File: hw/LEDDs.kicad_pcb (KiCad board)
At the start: 2 copper layers, 95 x 46 mm, 87 parts, among them J1 Screw_Terminal_01x02, J2 Conn_01x01, J3 Conn_01x06, J4 Screw_Terminal_01x02, K1 Relay_DPDT, Q10 MMBT3904, Q11 MMBT3906, Q13 IPN80R900P7, Q14 IPN80R900P7, Q2 BC846SF, Q8 MMBT3904, Q9 MMBT3904, U1 esp-12f, U2 PC817XI, U3 H11L1SR2M, U4 PC817XI

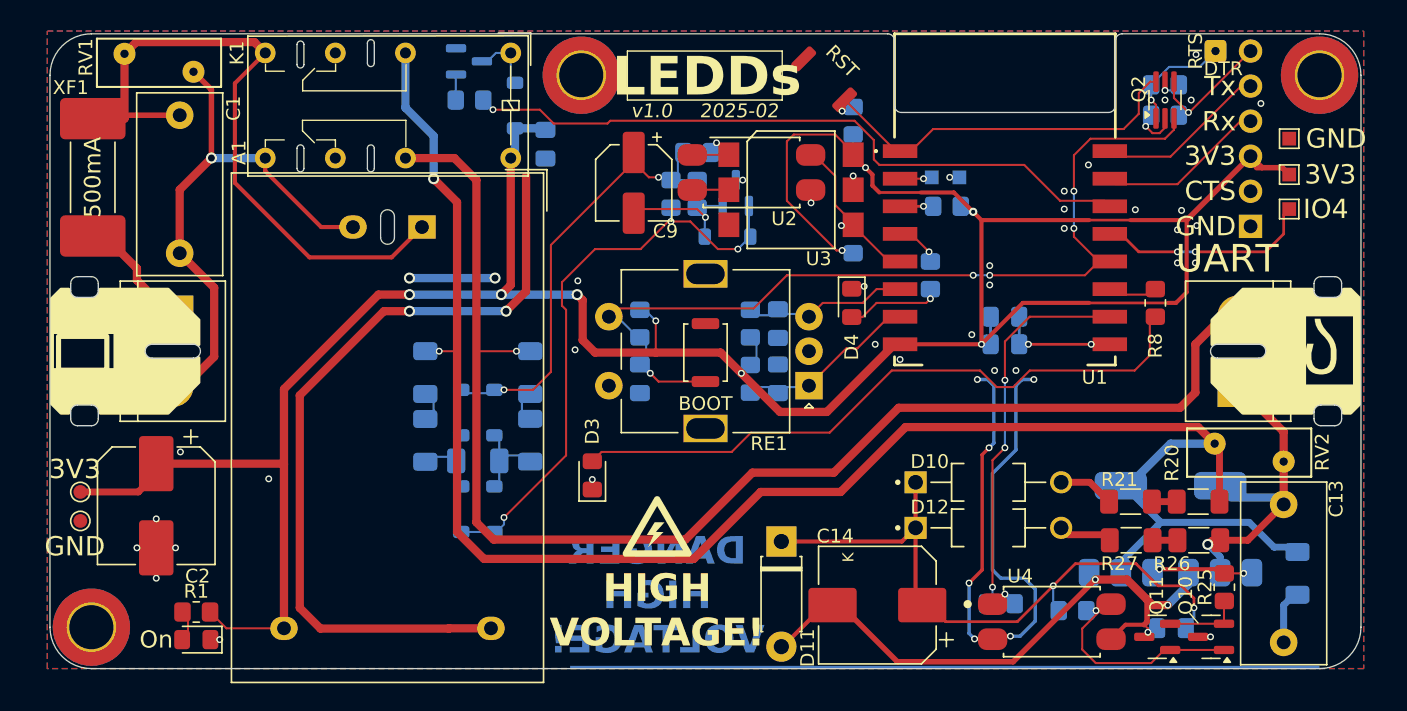
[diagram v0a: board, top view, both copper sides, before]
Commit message: V2.0 (#2)
* **Hardware & Mechanical Design**
  * Updated design files and exports.
  * Split chassis and top plate into variants.
  * Changed enclosure folder structure.
  * Hid alignment/dimension layers; removed duplicate models.
  * Added mechanical parts and notes to schematics.

* **Firmware**
  * Updated firmware and added new versions.
  * Introduced firmware variants and consolidated them into packages.
  * Added common.yaml.
  * Moved effects out of packages.

* **Project Structure & Tooling**
  * Added BOM exports and fixed script permissions.
  * Updated and cleaned export folders.
  * Added ESPHome auto-generated `.gitignore`.
  * Fixed included libraries.
  * Miscellaneous corrections, reviews, merges, and cleanup commits.

* **Documentation & README**
  * Multiple revisions for clarity, formatting, structure, and consistency.
  * Added safety warnings for mains voltage operation.
  * Updated table of contents, badges, links, images, and repository structure sections.
  * Added roadmap, split release and change logs, reformatted release log.
  * Added links to schematic, PCB, BOMs, and iBOM.
  * Added additional documentation files.

* **Images, Photos & Media**
  * Updated, renamed, resized, and reformatted images.
  * Improved README image layout (width adjustments, centering, reduced size).
  * Added photos and screenshots across README and sub-readmes.
  * Added animations and animation exports; removed obsolete images.
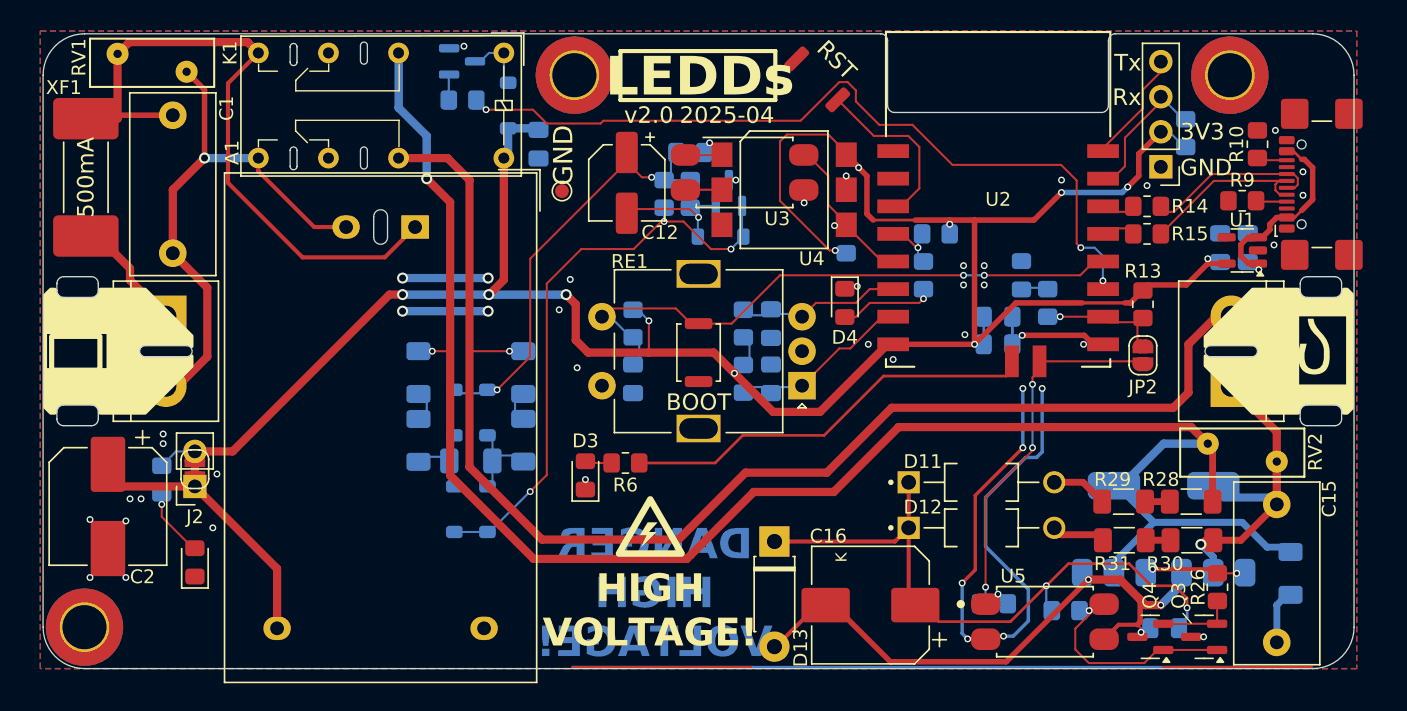
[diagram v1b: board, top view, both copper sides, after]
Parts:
- removed the Q2 at (133.3, 56.8)
- removed the R6 at (133.3, 57.9)
- removed the R7 at (133.3, 55.7)
- removed the TP1 at (54.7, 85.2)
- removed TP3: 3V3, TestPoint:TestPoint_Pad_1.0x1.0mm
- removed TP4: ADC, TestPoint:TestPoint_Pad_1.0x1.0mm
- removed TP5: GPIO4, TestPoint:TestPoint_Pad_1.0x1.0mm
- removed TP6, TP7: GND, TestPoint:TestPoint_Pad_1.0x1.0mm
- added C7: 1u, Capacitor_SMD:C_0805_2012Metric_Pad1.18x1.45mm_HandSolder, B.Cu at (139.3, 67.5)
- added C8: 1u, Capacitor_SMD:C_0805_2012Metric_Pad1.18x1.45mm_HandSolder, B.Cu at (137.3, 67.5)
- added D5: ~, LED_SMD:LED_0805_2012Metric_Pad1.15x1.40mm_HandSolder, B.Cu at (122.9, 69.5)
- added J3: USB_C_Receptacle_USB2.0_14P, Connector_USB:USB_C_Receptacle_GCT_USB4110, F.Cu at (145.8, 62.9)
- added JP1: SolderJumper_2_Bridged, Jumper:SolderJumper-2_P1.3mm_Bridged_RoundedPad1.0x1.5mm, F.Cu at (63.0, 83.5)
- added JP2: SolderJumper_2_Open, Jumper:SolderJumper-2_P1.3mm_Open_RoundedPad1.0x1.5mm, F.Cu at (131.7, 75.3)
- added R12: 20k, Resistor_SMD:R_0805_2012Metric_Pad1.20x1.40mm_HandSolder, B.Cu at (134.8, 59.2)
- added R13: 20k, Resistor_SMD:R_0805_2012Metric_Pad1.20x1.40mm_HandSolder, F.Cu at (131.7, 71.6)
- added R14: 0, Resistor_SMD:R_0805_2012Metric_Pad1.20x1.40mm_HandSolder, F.Cu at (132.0, 64.5)
- added R15: 0, Resistor_SMD:R_0805_2012Metric_Pad1.20x1.40mm_HandSolder, F.Cu at (132.0, 66.5)
- added R8: 240, Resistor_SMD:R_0805_2012Metric_Pad1.20x1.40mm_HandSolder, B.Cu at (124.8, 71.5)
- added R9: 5k1, Resistor_SMD:R_0805_2012Metric_Pad1.20x1.40mm_HandSolder, F.Cu at (138.9, 64.1)
- added U2: ESP32-C3-12F, ESP32-C3-12F:ESP32-C3-12F_RFS, F.Cu at (121.2, 64.0)
- C9: renamed from C8; value 100n -> 1u
- H1, H2, H3: value mounting hole -> 20mm
- J2: value Conn_01x01 -> Conn_01x02_Pin; footprint Connector_Wire:SolderWire-0.1sqmm_1x01_D0.4mm_OD1mm -> Connector_PinSocket_2.54mm:PinSocket_1x02_P2.54mm_Vertical
- J4: renamed from J3; footprint Connector_PinHeader_2.54mm:PinHeader_1x06_P2.54mm_Vertical -> Connector_PinHeader_2.54mm:PinHeader_1x04_P2.54mm_Vertical
- R1: value 120 -> 330; moved to B.Cu
- R10: value 20k -> 5k1; moved to F.Cu
- R16: renamed from R14; value 90k -> 91k
- R17: renamed from R15; value 90k -> 91k
- R18, R19: value 90k -> 91k
- RV1, RV2: value ~ -> 275V
- U1: value esp-12f -> AP2112K-3.3; footprint ESP-12F:esp12f -> Package_TO_SOT_SMD:SOT-23-5
- moved J2 80.4 mm to (63.0, 84.8), turned to 180 degrees
- moved TP1 42.3 mm to (89.6, 63.4), turned to 90 degrees
- moved R6 40.1 mm to (94.2, 83.1), turned to 0 degrees
- moved R10 29.3 mm to (140.0, 60.0), turned to 90 degrees
- moved U1 17.6 mm to (138.9, 67.7), turned to 180 degrees
- moved R1 9.92 mm to (60.6, 84.3), turned to 90 degrees
- moved J4 7.80 mm to (133.0, 61.6)
- moved H2 6.50 mm to (138.0, 55.0)
- moved D1 5.60 mm to (63.0, 90.3), turned to 90 degrees
- moved C2 3.50 mm to (56.7, 86.2)
- moved R11 2.15 mm to (116.7, 66.5)
- moved A1 0.50 mm to (79.0, 66.0)
- moved C1 0.50 mm to (61.4, 57.9)
- moved C10 0.50 mm to (121.2, 74.5)
- moved C11 0.50 mm to (83.0, 83.0)
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- renumbered C7 to C10, C10 to C11, C9 to C12, C11 to C13, C12 to C14, C13 to C15, C14 to C16, C5 to C4, C6 to C5, C4 to C6, D7 to D10, D10 to D11, D11 to D13, D5 to D6, D6 to D7, J4 to J5, Q8 to Q1, Q9 to Q2, Q10 to Q3, Q11 to Q4, Q13 to Q5, Q14 to Q6, R17 to R20, R16 to R21, R13 to R22, R12 to R23, R22 to R25, R25 to R26, R23 to R27, R20 to R28, R21 to R29, R26 to R30, R27 to R31, R8 to R6, R9 to R7, TP2 to TP1, U2 to U3, U3 to U4, U4 to U5
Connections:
- A1 pad 4: +3V3 -> Net-(A1-+Vout)
- C2 pad 1: +3V3 -> Net-(A1-+Vout)
- J2 pad 1: /MCU/rts -> Net-(A1-+Vout)
- J4 pad 2: /MCU/ cts -> +3V3
- J4 pad 3: +3V3 -> /MCU/mcu_rx
- J4 pad 4: /MCU/mcu_rx -> /MCU/mcu_tx
- R10 pad 1: /MCU/mcu_rst -> Net-(J3-CC2)
- R10 pad 2: +3V3 -> GNDD
- R11 pad 1: Net-(U1-EN) -> /MCU/led_2
- SW2 pad 1: /MCU/mcu_boot -> GNDD
- SW2 pad 2: GNDD -> /MCU/mcu_boot
- U1 pad 1: /MCU/mcu_rst -> +5V
- U1 pad 2: /MCU/adc -> GNDD
- U1 pad 3: Net-(U1-EN) -> +5V
- U1 pad 4: /MCU/led_2 -> unconnected-(U1-NC-Pad4)
- U1 pad 5: /Dimmer/z-c -> +3V3
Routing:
- net GNDD: track 119.3 -> 66.6 mm, vias 47 -> 43
- net Net-(D3-A): track 47.0 -> 1.95 mm
- net +3V3: track 208.2 -> 174.8 mm, vias 9 -> 12
- net /MCU/led_1: track 2.50 -> 29.4 mm
- net /MCU/mcu_boot: track 62.0 -> 41.2 mm, vias 5 -> 2
- net Net-(A1-+Vout): track 0.00 -> 18.9 mm
- net +5V: track 0.00 -> 15.4 mm, vias 0 -> 1
- net /MCU/mcu_rst: track 27.4 -> 12.8 mm, vias 1 -> 0
- net /MCU/gpio4: track 14.3 -> 0.00 mm, vias 2 -> 0
- net /MCU/USB_DN: track 0.00 -> 13.0 mm
- net /MCU/USB_DP: track 0.00 -> 12.7 mm
- net /MCU/dtr: track 9.21 -> 0.00 mm, vias 1 -> 0
- net /MCU/relay: track 49.0 -> 58.1 mm, vias 1 -> 3
- net /MCU/rts: track 8.55 -> 0.00 mm, vias 1 -> 0
- net /MCU/led_3: track 0.00 -> 8.52 mm, vias 0 -> 1
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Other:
- outline, holes or cut-outs redrawn
- board text added: "2025-04"
- board text added: "v2.0"
- board text removed: "2025-02"
- board text removed: "CTS"
- board text removed: "DTR"
- board text removed: "RTS"
- board text removed: "v1.0"
